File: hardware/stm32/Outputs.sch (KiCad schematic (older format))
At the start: 0 parts

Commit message: bluepill Schematics 0.99
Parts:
- added C1: 220u, Capacitors_THT:CP_Radial_D10.0mm_P3.50mm, symbol CP_Small
- added J10, J11, J12, J13, J6, J8, J9: Screw_Terminal_01x02, TerminalBlock:TerminalBlock_bornier-2_P5.08mm, symbol Screw_Terminal_01x02
- added J7: Conn_01x02, Connectors_JST:JST_EH_B02B-EH-A_02x2.50mm_Straight, symbol Conn_01x02
- added Q1, Q2, Q3, Q4, Q5, Q6: Q_NMOS_GSD, TO_SOT_Packages_SMD:SOT-23, symbol Q_NMOS_GSD
- added R13, R14, R15, R16, R17, R18, R19, R20, R21, R22, R23, R24: 4.7k, Resistors_SMD:R_0603_HandSoldering, symbol R_Small
- added U10, U11, U5, U6, U7, U8, U9: PC817, Housings_DIP:DIP-4_W7.62mm, symbol PC817
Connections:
- new net: Q6.1 (G), R18.1, U11.3
- new net: R24.1, U11.4
- new net: J13.2 (Pin_2), Q6.3 (D)
- new net: Q5.1 (G), R17.1, U10.3
- new net: R23.1, U10.4
- new net: J12.2 (Pin_2), Q5.3 (D)
- new net: Q4.1 (G), R16.1, U9.3
- new net: R22.1, U9.4
- new net: J11.2 (Pin_2), Q4.3 (D)
- new net: Q3.1 (G), R15.1, U8.3
- new net: R21.1, U8.4
- new net: J10.2 (Pin_2), Q3.3 (D)
- new net: Q2.1 (G), R14.1, U7.3
- new net: R20.1, U7.4
- new net: J9.2 (Pin_2), Q2.3 (D)
- new net: Q1.1 (G), R13.1, U6.3
- new net: R19.1, U6.4
- new net: J8.2 (Pin_2), Q1.3 (D)
- new net: J7.2 (Pin_2), U5.3
- new net: J7.1 (Pin_1), U5.4
- new net +12V: C1.1, J10.1 (Pin_1), J11.1 (Pin_1), J12.1 (Pin_1), J13.1 (Pin_1), J6.1 (Pin_1), J8.1 (Pin_1), J9.1 (Pin_1), R19.2, R20.2, R21.2, R22.2, R23.2, R24.2
- new net +3V3: U10.1, U11.1, U5.1, U6.1, U7.1, U8.1, U9.1
- new net GNDPWR: C1.2, J6.2 (Pin_2), Q1.2 (S), Q2.2 (S), Q3.2 (S), Q4.2 (S), Q5.2 (S), Q6.2 (S), R13.2, R14.2, R15.2, R16.2, R17.2, R18.2
- new net IG: U11.2
- new net IR: U9.2
- new net IY: U10.2
- new net OG: U8.2
- new net OPEN: U5.2
- new net OR: U6.2
- new net OY: U7.2

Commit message: bluepill PCB progress
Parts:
- added D1, D2, D3, D4, D5, D6: 1N4148, Diodes_SMD:D_MiniMELF, symbol D_Small
- Q1, Q2, Q3, Q4, Q5, Q6: value Q_NMOS_GSD -> IRLML2502
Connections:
- net +12V: now also D1.1 (K), D2.1 (K), D3.1 (K), D4.1 (K), D5.1 (K), D6.1 (K)
- net at J13.2 (Pin_2), Q6.3 (D): now also D6.2 (A)
- net at J12.2 (Pin_2), Q5.3 (D): now also D5.2 (A)
- net at J11.2 (Pin_2), Q4.3 (D): now also D4.2 (A)
- net at J10.2 (Pin_2), Q3.3 (D): now also D3.2 (A)
- net at J9.2 (Pin_2), Q2.3 (D): now also D2.2 (A)
- net at J8.2 (Pin_2), Q1.3 (D): now also D1.2 (A)
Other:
- moved on the sheet: C1, J10, J11, J12, J13, J6, J7, J8, J9, Q1, Q2, Q3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

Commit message: bluepill: PCB 0.9
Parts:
- U5: footprint Housings_DIP:DIP-4_W7.62mm -> Housings_DIP:DIP-4_W7.62mm_LongPads
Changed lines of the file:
@@
 F 0 "U5" H 9200 2700 50  0000 L CNN
 F 1 "PC817" H 9400 2700 50  0000 L CNN
-F 2 "Housings_DIP:DIP-4_W7.62mm" H 9200 2300 50  0001 L CIN
+F 2 "Housings_DIP:DIP-4_W7.62mm_LongPads" H 9200 2300 50  0001 L CIN
 F 3 "" H 9400 2500 50  0001 L CNN
 	1    9400 2500
@@
 $EndComp
 $Comp
-L +3.3V #PWR031
+L +3.3V #PWR46
 U 1 1 5A5FF7EF
 P 9000 2200
-F 0 "#PWR031" H 9000 2050 50  0001 C CNN
+F 0 "#PWR46" H 9000 2050 50  0001 C CNN
 F 1 "+3.3V" H 9000 2340 50  0000 C CNN
 F 2 "" H 9000 2200 50  0001 C CNN
@@
 $EndComp
 $Comp
-L +12V #PWR033
+L +12V #PWR47
 U 1 1 5A600289
 P 9500 1000
-F 0 "#PWR033" H 9500 850 50  0001 C CNN
+F 0 "#PWR47" H 9500 850 50  0001 C CNN
 F 1 "+12V" H 9500 1140 50  0000 C CNN
 F 2 "" H 9500 1000 50  0001 C CNN
@@
 $EndComp
 $Comp
-L GNDPWR #PWR034
+L GNDPWR #PWR45
 U 1 1 5A601D85
 P 7350 2950
-F 0 "#PWR034" H 7350 2750 50  0001 C CNN
+F 0 "#PWR45" H 7350 2750 50  0001 C CNN
 F 1 "GNDPWR" H 7350 2820 50  0000 C CNN
 F 2 "" H 7350 2900 50  0001 C CNN
@@
 $EndComp
 $Comp
-L GNDPWR #PWR035
+L GNDPWR #PWR49
 U 1 1 5A6021DD
 P 9650 1550
-F 0 "#PWR035" H 9650 1350 50  0001 C CNN
+F 0 "#PWR49" H 9650 1350 50  0001 C CNN
 F 1 "GNDPWR" H 9850 1550 50  0000 C CNN
 F 2 "" H 9650 1500 50  0001 C CNN
@@
 $EndComp
 $Comp
-L GNDPWR #PWR036
+L GNDPWR #PWR48
 U 1 1 5A6022C8
 P 9500 1550
-F 0 "#PWR036" H 9500 1350 50  0001 C CNN
+F 0 "#PWR48" H 9500 1350 50  0001 C CNN
 F 1 "GNDPWR" H 9300 1550 50  0000 C CNN
 F 2 "" H 9500 1500 50  0001 C CNN
@@
 $EndComp
 $Comp
-L +3.3V #PWR?
+L +3.3V #PWR41
 U 1 1 5A6240B1
 P 5950 2100
-F 0 "#PWR?" H 5950 1950 50  0001 C CNN
+F 0 "#PWR41" H 5950 1950 50  0001 C CNN
 F 1 "+3.3V" H 5950 2240 50  0000 C CNN
 F 2 "" H 5950 2100 50  0001 C CNN
@@
 $EndComp
 $Comp
-L +12V #PWR?
+L +12V #PWR43
 U 1 1 5A6249DA
 P 6950 2100
-F 0 "#PWR?" H 6950 1950 50  0001 C CNN
+F 0 "#PWR43" H 6950 1950 50  0001 C CNN
 F 1 "+12V" H 6950 2240 50  0000 C CNN
 F 2 "" H 6950 2100 50  0001 C CNN
@@
 Connection ~ 4850 2300
 $Comp
-L +3.3V #PWR?
+L +3.3V #PWR40
 U 1 1 5A628130
 P 5950 850
-F 0 "#PWR?" H 5950 700 50  0001 C CNN
+F 0 "#PWR40" H 5950 700 50  0001 C CNN
 F 1 "+3.3V" H 5950 990 50  0000 C CNN
 F 2 "" H 5950 850 50  0001 C CNN
@@
 $EndComp
 $Comp
-L +12V #PWR?
+L +12V #PWR42
 U 1 1 5A6281B3
 P 6950 850
-F 0 "#PWR?" H 6950 700 50  0001 C CNN
+F 0 "#PWR42" H 6950 700 50  0001 C CNN
 F 1 "+12V" H 6950 990 50  0000 C CNN
 F 2 "" H 6950 850 50  0001 C CNN
@@
 	5950 1150 5950 850
 $Comp
-L GNDPWR #PWR?
+L GNDPWR #PWR44
 U 1 1 5A628708
 P 7350 1750
-F 0 "#PWR?" H 7350 1550 50  0001 C CNN
+F 0 "#PWR44" H 7350 1550 50  0001 C CNN
 F 1 "GNDPWR" H 7350 1620 50  0000 C CNN
 F 2 "" H 7350 1700 50  0001 C CNN
@@
 $EndComp
 $Comp
-L GNDPWR #PWR?
+L GNDPWR #PWR38
 U 1 1 5A6287DB
 P 4850 1750
-F 0 "#PWR?" H 4850 1550 50  0001 C CNN
+F 0 "#PWR38" H 4850 1550 50  0001 C CNN
 F 1 "GNDPWR" H 4850 1620 50  0000 C CNN
 F 2 "" H 4850 1700 50  0001 C CNN
@@
 $EndComp
 $Comp
-L GNDPWR #PWR?
+L GNDPWR #PWR39
 U 1 1 5A628886
 P 4850 2950
-F 0 "#PWR?" H 4850 2750 50  0001 C CNN
+F 0 "#PWR39" H 4850 2750 50  0001 C CNN
 F 1 "GNDPWR" H 4850 2820 50  0000 C CNN
 F 2 "" H 4850 2900 50  0001 C CNN
@@
 $EndComp
 $Comp
-L GNDPWR #PWR?
+L GNDPWR #PWR32
 U 1 1 5A628909
 P 2350 1750
-F 0 "#PWR?" H 2350 1550 50  0001 C CNN
+F 0 "#PWR32" H 2350 1550 50  0001 C CNN
 F 1 "GNDPWR" H 2350 1620 50  0000 C CNN
 F 2 "" H 2350 1700 50  0001 C CNN
@@
 $EndComp
 $Comp
-L GNDPWR #PWR?
+L GNDPWR #PWR33
 U 1 1 5A62898C
 P 2350 2950
-F 0 "#PWR?" H 2350 2750 50  0001 C CNN
+F 0 "#PWR33" H 2350 2750 50  0001 C CNN
 F 1 "GNDPWR" H 2350 2820 50  0000 C CNN
 F 2 "" H 2350 2900 50  0001 C CNN
@@
 $EndComp
 $Comp
-L +3.3V #PWR?
+L +3.3V #PWR34
 U 1 1 5A628A0F
 P 3450 850
-F 0 "#PWR?" H 3450 700 50  0001 C CNN
+F 0 "#PWR34" H 3450 700 50  0001 C CNN
 F 1 "+3.3V" H 3450 990 50  0000 C CNN
 F 2 "" H 3450 850 50  0001 C CNN
@@
 $EndComp
 $Comp
-L +3.3V #PWR?
+L +3.3V #PWR35
 U 1 1 5A628A92
 P 3450 2100
-F 0 "#PWR?" H 3450 1950 50  0001 C CNN
+F 0 "#PWR35" H 3450 1950 50  0001 C CNN
 F 1 "+3.3V" H 3450 2240 50  0000 C CNN
 F 2 "" H 3450 2100 50  0001 C CNN
@@
 $EndComp
 $Comp
-L +12V #PWR?
+L +12V #PWR36
 U 1 1 5A628B15
 P 4450 850
-F 0 "#PWR?" H 4450 700 50  0001 C CNN
+F 0 "#PWR36" H 4450 700 50  0001 C CNN
 F 1 "+12V" H 4450 990 50  0000 C CNN
 F 2 "" H 4450 850 50  0001 C CNN
@@
 $EndComp
 $Comp
-L +12V #PWR?
+L +12V #PWR37
 U 1 1 5A628B98
 P 4450 2100
-F 0 "#PWR?" H 4450 1950 50  0001 C CNN
+F 0 "#PWR37" H 4450 1950 50  0001 C CNN
 F 1 "+12V" H 4450 2240 50  0000 C CNN
 F 2 "" H 4450 2100 50  0001 C CNN
@@
 Connection ~ 4850 2900
 $Comp
-L +12V #PWR?
+L +12V #PWR30
 U 1 1 5A629244
 P 1950 850
-F 0 "#PWR?" H 1950 700 50  0001 C CNN
+F 0 "#PWR30" H 1950 700 50  0001 C CNN
 F 1 "+12V" H 1950 990 50  0000 C CNN
 F 2 "" H 1950 850 50  0001 C CNN
@@
 $EndComp
 $Comp
-L +12V #PWR?
+L +12V #PWR31
 U 1 1 5A6292C7
 P 1950 2050
-F 0 "#PWR?" H 1950 1900 50  0001 C CNN
+F 0 "#PWR31" H 1950 1900 50  0001 C CNN
 F 1 "+12V" H 1950 2190 50  0000 C CNN
 F 2 "" H 1950 2050 50  0001 C CNN
@@
 $EndComp
 $Comp
-L +3.3V #PWR?
+L +3.3V #PWR28
 U 1 1 5A62934A
 P 950 850
-F 0 "#PWR?" H 950 700 50  0001 C CNN
+F 0 "#PWR28" H 950 700 50  0001 C CNN
 F 1 "+3.3V" H 950 990 50  0000 C CNN
 F 2 "" H 950 850 50  0001 C CNN
@@
 $EndComp
 $Comp
-L +3.3V #PWR?
+L +3.3V #PWR29
 U 1 1 5A6293CD
 P 950 2050
-F 0 "#PWR?" H 950 1900 50  0001 C CNN
+F 0 "#PWR29" H 950 1900 50  0001 C CNN
 F 1 "+3.3V" H 950 2190 50  0000 C CNN
 F 2 "" H 950 2050 50  0001 C CNN

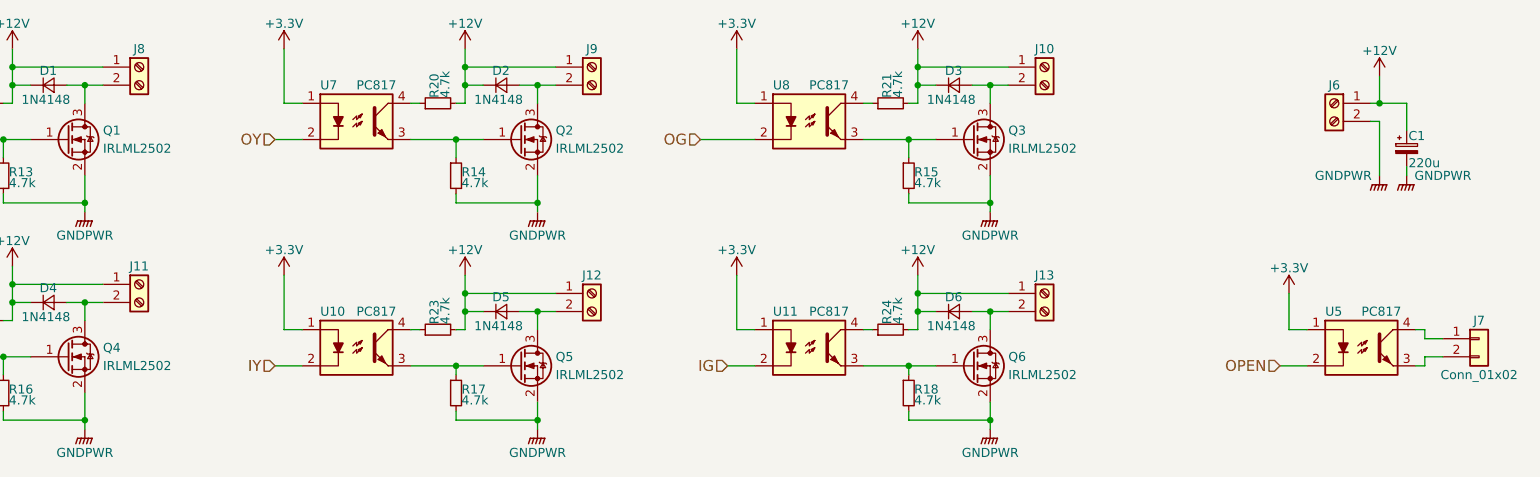
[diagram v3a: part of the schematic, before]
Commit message: bluepill PCB: SD Card socket turned around
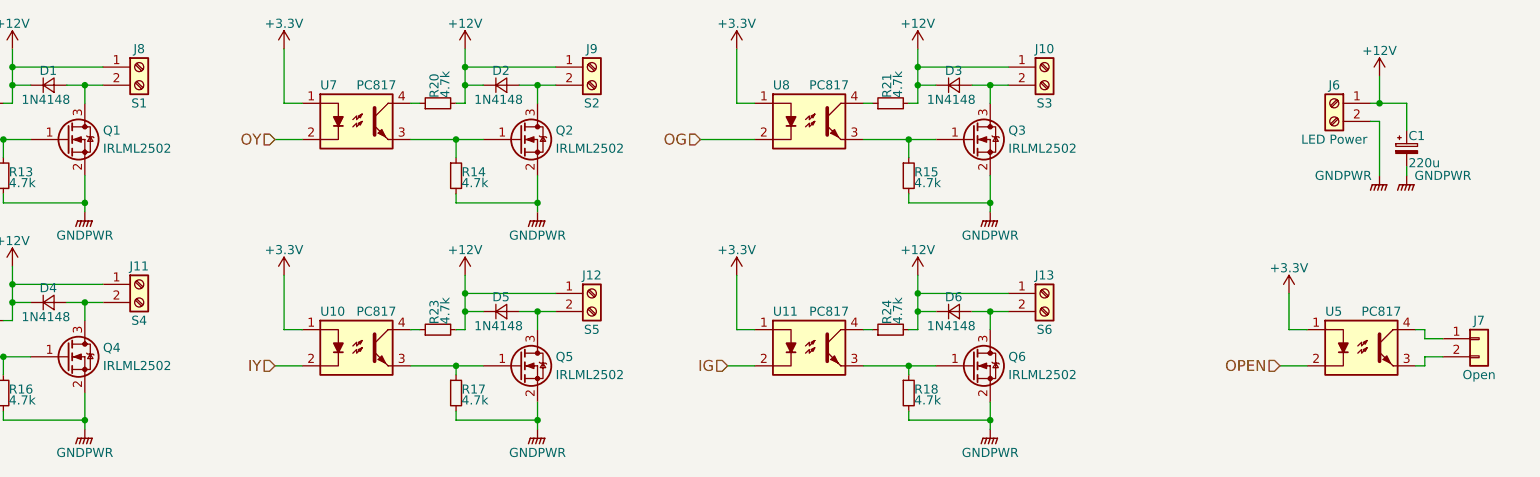
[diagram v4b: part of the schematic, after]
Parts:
- J10: value Screw_Terminal_01x02 -> S3
- J11: value Screw_Terminal_01x02 -> S4
- J12: value Screw_Terminal_01x02 -> S5
- J13: value Screw_Terminal_01x02 -> S6
- J6: value Screw_Terminal_01x02 -> LED Power
- J7: value Conn_01x02 -> Open
- J8: value Screw_Terminal_01x02 -> S1
- J9: value Screw_Terminal_01x02 -> S2
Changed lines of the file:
@@
 P 7650 2200
 F 0 "J13" H 7650 2300 50  0000 C CNN
-F 1 "Screw_Terminal_01x02" H 7650 2000 50  0001 C CNN
+F 1 "S6" H 7650 2000 50  0000 C CNN
 F 2 "TerminalBlock:TerminalBlock_bornier-2_P5.08mm" H 7650 2200 50  0001 C CNN
 F 3 "" H 7650 2200 50  0001 C CNN
@@
 P 5150 2200
 F 0 "J12" H 5150 2300 50  0000 C CNN
-F 1 "Screw_Terminal_01x02" H 5150 2000 50  0001 C CNN
+F 1 "S5" H 5150 2000 50  0000 C CNN
 F 2 "TerminalBlock:TerminalBlock_bornier-2_P5.08mm" H 5150 2200 50  0001 C CNN
 F 3 "" H 5150 2200 50  0001 C CNN
@@
 P 2650 2150
 F 0 "J11" H 2650 2250 50  0000 C CNN
-F 1 "Screw_Terminal_01x02" H 2650 1950 50  0001 C CNN
+F 1 "S4" H 2650 1950 50  0000 C CNN
 F 2 "TerminalBlock:TerminalBlock_bornier-2_P5.08mm" H 2650 2150 50  0001 C CNN
 F 3 "" H 2650 2150 50  0001 C CNN
@@
 P 7650 950
 F 0 "J10" H 7650 1050 50  0000 C CNN
-F 1 "Screw_Terminal_01x02" H 7650 750 50  0001 C CNN
+F 1 "S3" H 7650 750 50  0000 C CNN
 F 2 "TerminalBlock:TerminalBlock_bornier-2_P5.08mm" H 7650 950 50  0001 C CNN
 F 3 "" H 7650 950 50  0001 C CNN
@@
 P 5150 950
 F 0 "J9" H 5150 1050 50  0000 C CNN
-F 1 "Screw_Terminal_01x02" H 5150 750 50  0001 C CNN
+F 1 "S2" H 5150 750 50  0000 C CNN
 F 2 "TerminalBlock:TerminalBlock_bornier-2_P5.08mm" H 5150 950 50  0001 C CNN
 F 3 "" H 5150 950 50  0001 C CNN
@@
 P 2650 950
 F 0 "J8" H 2650 1050 50  0000 C CNN
-F 1 "Screw_Terminal_01x02" H 2650 750 50  0001 C CNN
+F 1 "S1" H 2650 750 50  0000 C CNN
 F 2 "TerminalBlock:TerminalBlock_bornier-2_P5.08mm" H 2650 950 50  0001 C CNN
 F 3 "" H 2650 950 50  0001 C CNN
@@
 P 10050 2450
 F 0 "J7" H 10050 2550 50  0000 C CNN
-F 1 "Conn_01x02" H 10050 2250 50  0000 C CNN
+F 1 "Open" H 10050 2250 50  0000 C CNN
 F 2 "Connectors_JST:JST_EH_B02B-EH-A_02x2.50mm_Straight" H 10050 2450 50  0001 C CNN
 F 3 "" H 10050 2450 50  0001 C CNN
@@
 P 9250 1150
 F 0 "J6" H 9250 1250 50  0000 C CNN
-F 1 "Screw_Terminal_01x02" H 9250 950 50  0001 C CNN
+F 1 "LED Power" H 9250 950 50  0000 C CNN
 F 2 "TerminalBlock:TerminalBlock_bornier-2_P5.08mm" H 9250 1150 50  0001 C CNN
 F 3 "" H 9250 1150 50  0001 C CNN
